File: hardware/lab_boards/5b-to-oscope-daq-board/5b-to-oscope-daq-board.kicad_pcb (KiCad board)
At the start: 2 copper layers, 17 parts, among them J1 OSCOPE 3, J10 OSCOPE 6, J11 OSCOPE 1, J12 DAQ 6, J13 TX_SHUNT, J14 OSCOPE 7, J15 DAQ 7, J16 OSCOPE 8, J17 5B P1, J18 TO DAQ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

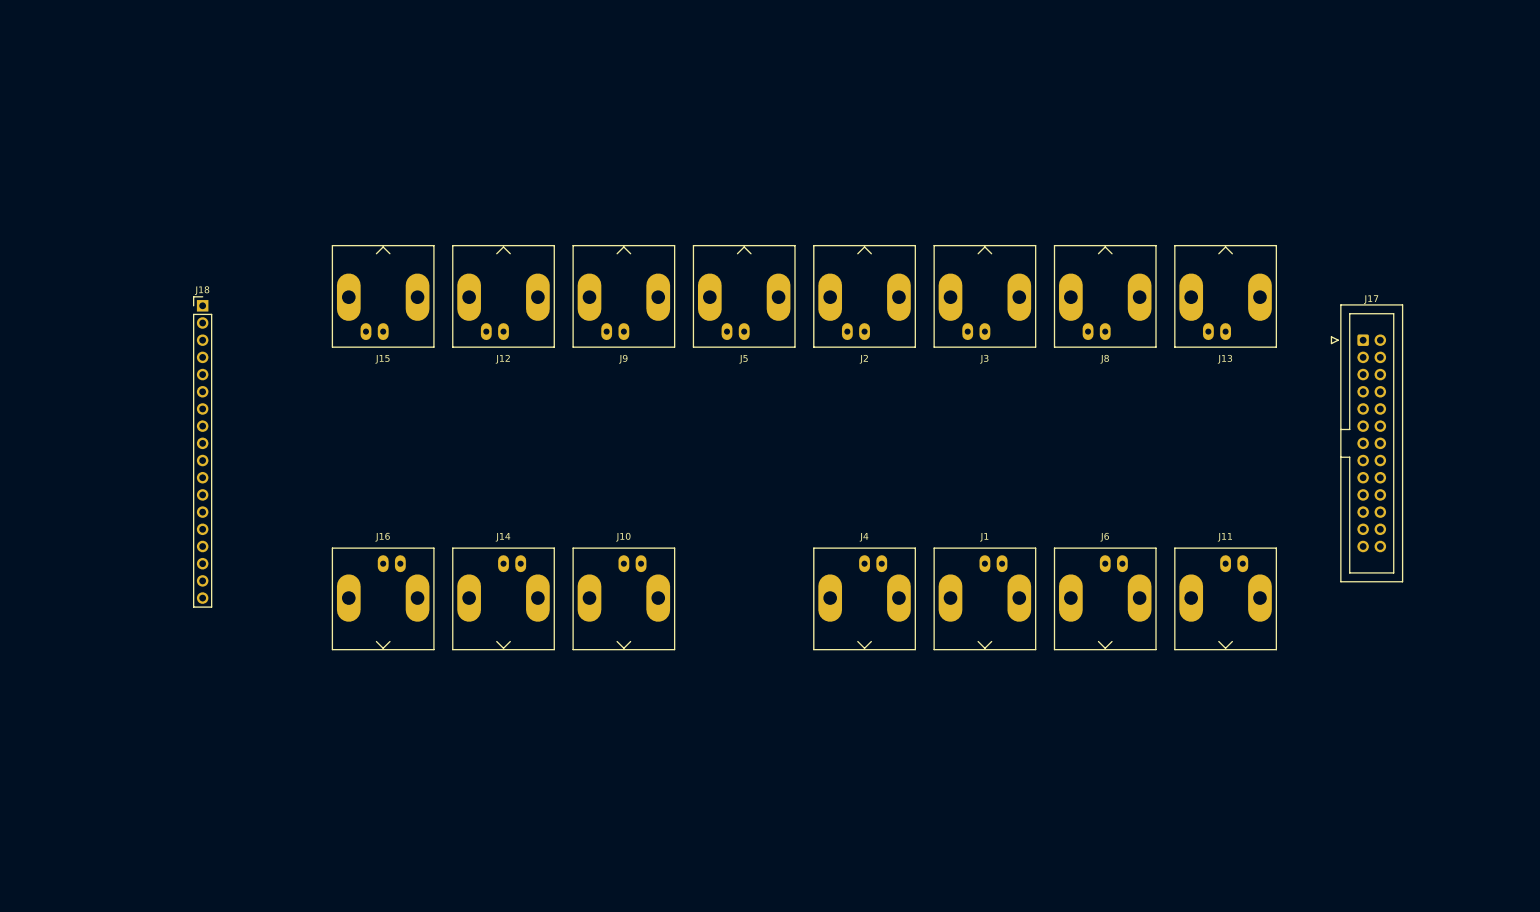
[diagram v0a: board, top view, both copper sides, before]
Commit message: Added an AWG to TX array connection and calibration board project
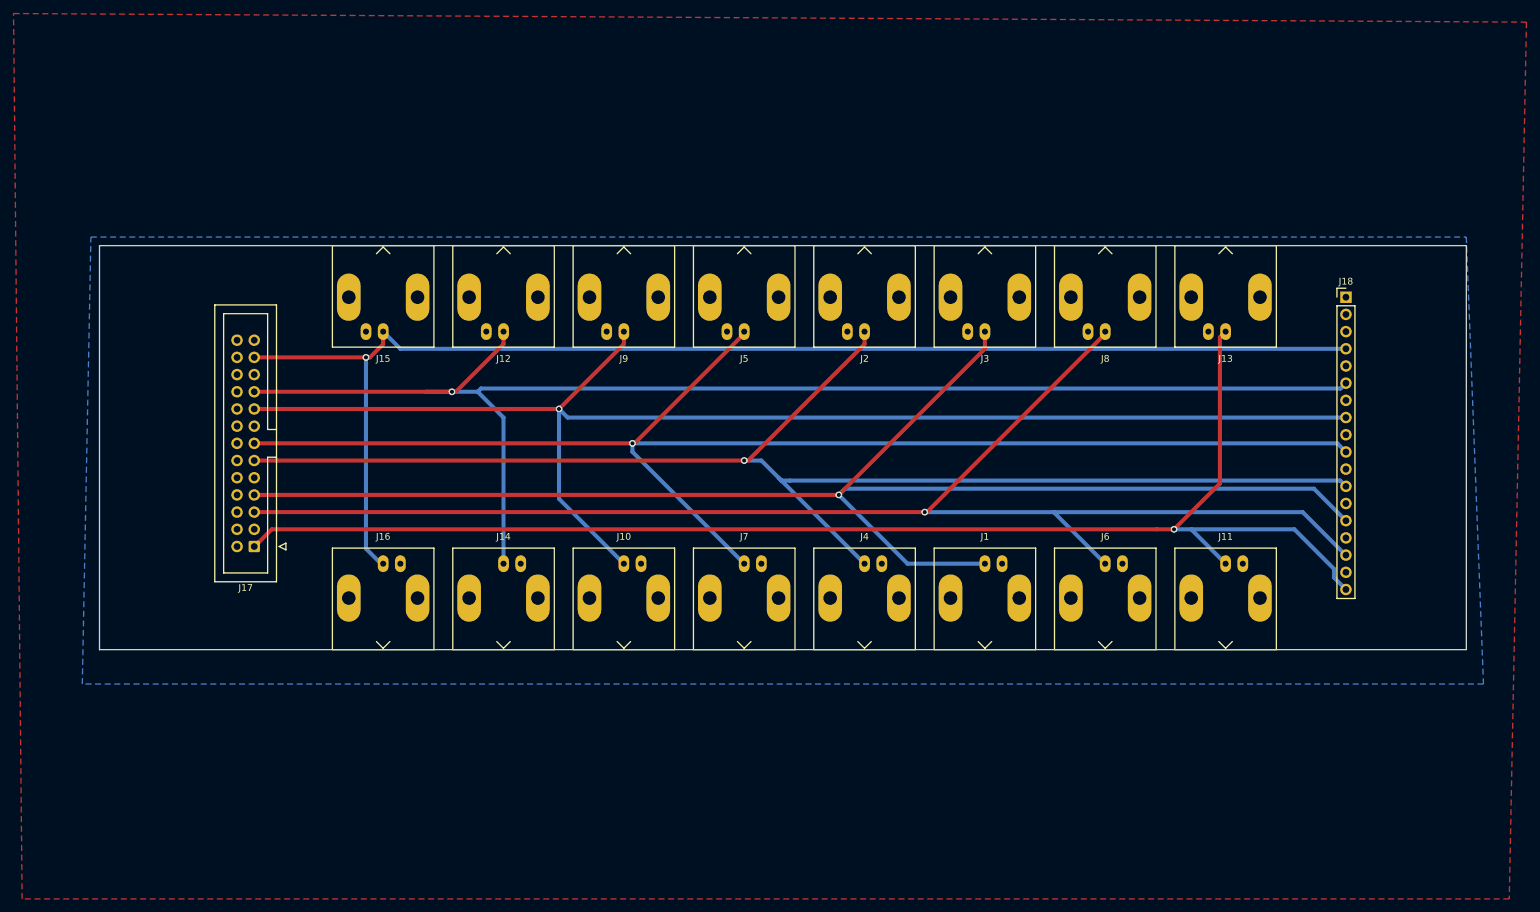
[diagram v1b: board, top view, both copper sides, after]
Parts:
- added J7: OSCOPE5, Connector_Coaxial:BNC_Amphenol_B6252HB-NPP3G-50_Horizontal, F.Cu at (146.1, 106.7)
- moved J18 168.9 mm to (234.9, 67.3)
- moved J17 166.6 mm to (73.7, 104.1), turned to 180 degrees
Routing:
- net /CHANNEL2: track 0.00 -> 222.5 mm, vias 0 -> 1
- net /CHANNEL1: track 0.00 -> 212.6 mm, vias 0 -> 1
- net /CHANNEL4: track 0.00 -> 210.0 mm, vias 0 -> 1
- net /CHANNEL3: track 0.00 -> 207.6 mm, vias 0 -> 1
- net /CHANNEL0: track 0.00 -> 206.3 mm, vias 0 -> 1
- net /CHANNEL6: track 0.00 -> 205.0 mm, vias 0 -> 1
- net /CHANNEL5: track 0.00 -> 204.0 mm, vias 0 -> 1
- net /CHANNEL7: track 0.00 -> 196.7 mm, vias 0 -> 1
- added copper zone on B.Cu, net GNDS
- added copper zone on F.Cu, net GNDS
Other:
- board outline added: 201.9 x 59.7 mm
- net class Default: clearance 0.2 -> 0.6; trace_width 0.25 -> 0.6; via_dia 0.8 -> 1; via_drill 0.4 -> 0.6
- rule trace_clearance: 0.2 -> 0.6
- rule trace_min: 0.2 -> 0.4
- rule via_min_drill: 0.3 -> 0.2
- rule via_min_size: 0.4 -> 0.6
